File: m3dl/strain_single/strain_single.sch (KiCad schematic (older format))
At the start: 66 parts, among them IC1 AD8226, IC2 AD8541, IC3 AD8226, IC4 AD8541, IC5 AD8656, IC6 AD8226, IC7 AD8541, IC8 AD8656, IC9 AD8656, J1 WEST TOP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

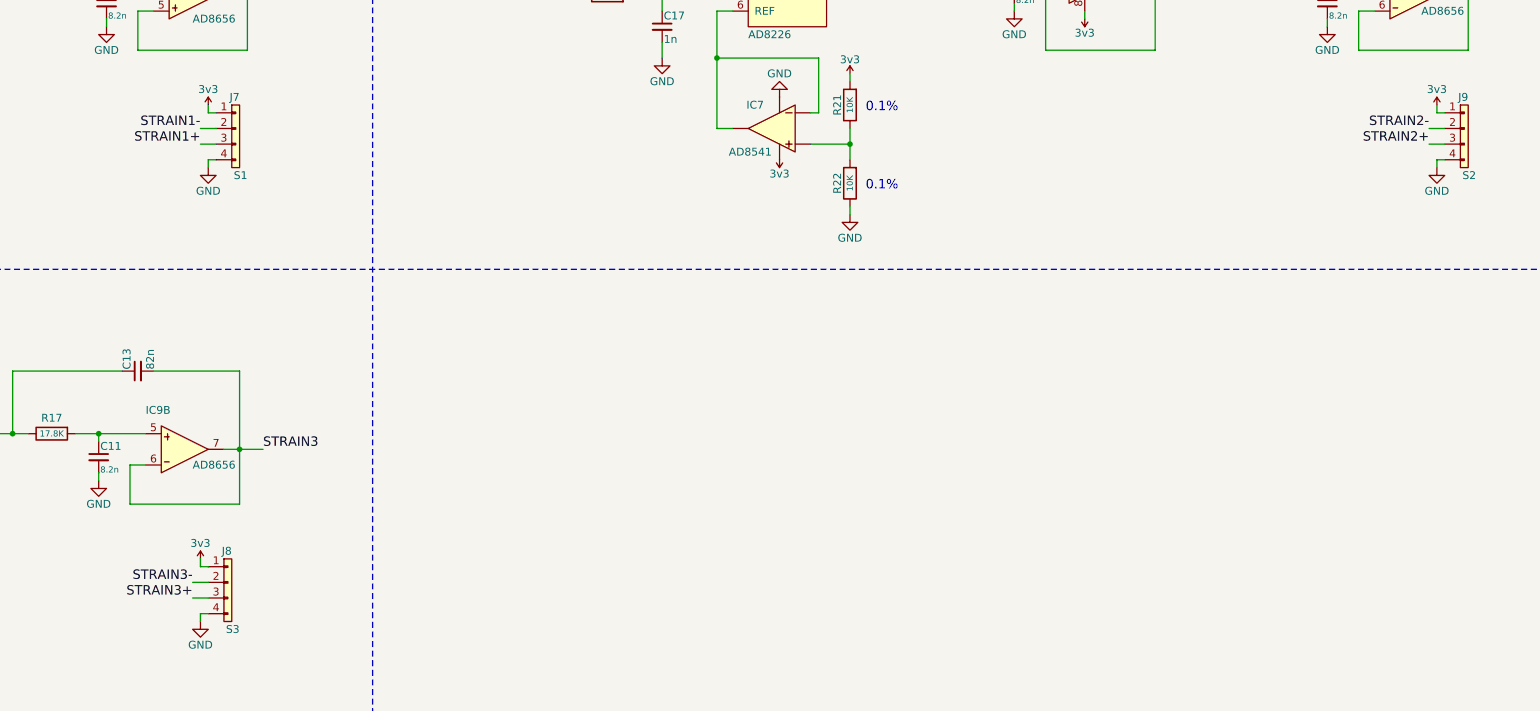
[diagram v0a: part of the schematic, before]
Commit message: Started Strain Gauge PCB Layout
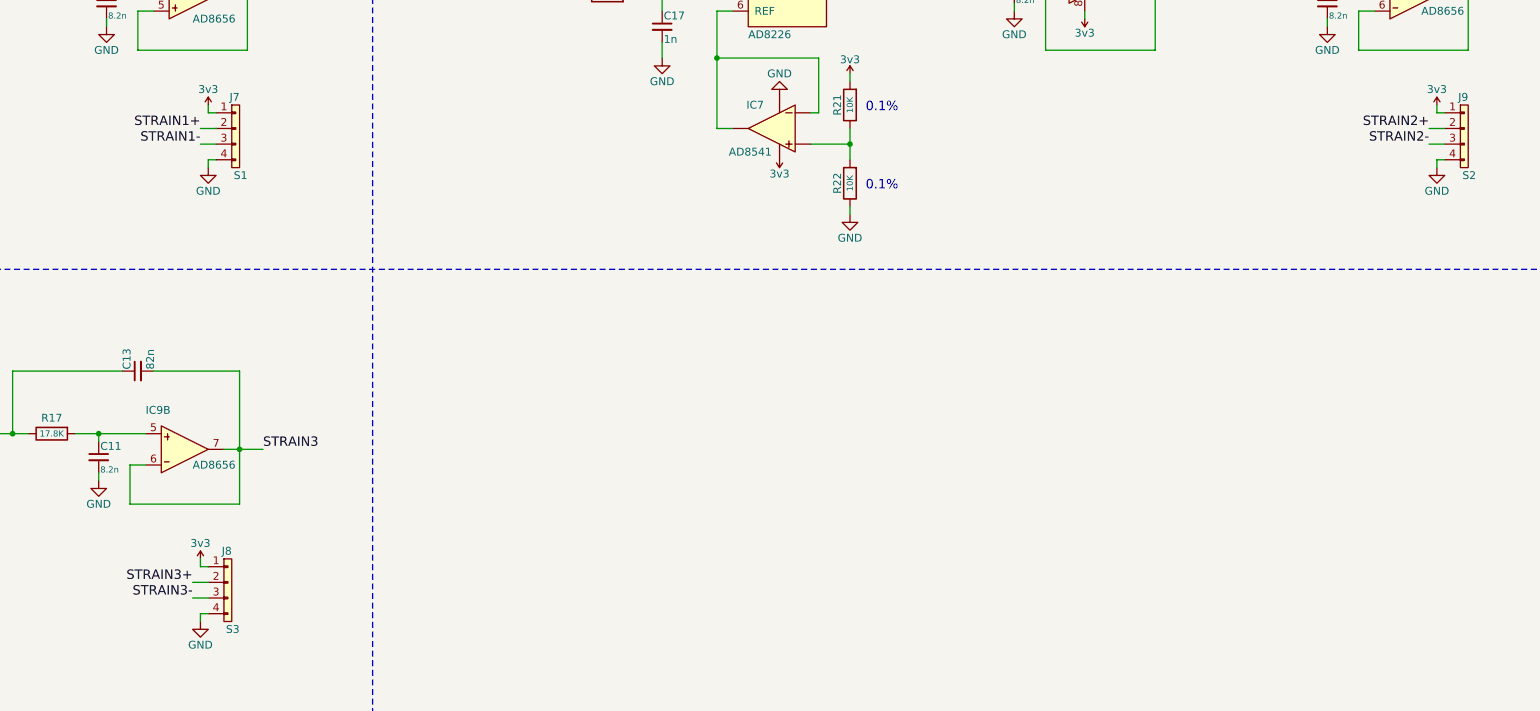
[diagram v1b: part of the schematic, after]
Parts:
- J7, J8, J9: footprint Connectors_Molex:Connector_Molex_PicoBlade_53047-0410 -> Connectors_Molex:Connector_Molex_PicoBlade_53048-0410
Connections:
- net STRAIN1+: now also J7.2; no longer J7.3
- net STRAIN1-: now also J7.3; no longer J7.2
- net STRAIN2+: now also J9.2; no longer J9.3
- net STRAIN2-: now also J9.3; no longer J9.2
- net STRAIN3+: now also J8.2; no longer J8.3
- net STRAIN3-: now also J8.3; no longer J8.2

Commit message: Finished routing Strain Gauge PCB - Needs Silkscreen
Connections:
- net STRAIN1: now also IC5.6 (-IN); no longer IC5.5 (+IN)
- net at C12.1, R18.2: now also IC5.5 (+IN); no longer IC5.6 (-IN)
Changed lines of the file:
@@
 F 4 "1858055" H 6950 1150 50  0001 L CNN "Farnell"
 	2    6950 1650
-	1    0    0    -1
+	1    0    0    1
 $EndComp
 Text Label 1550 1450 2    60   ~ 0

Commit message: Finished routing Pressure PCB - Needs Silkscreen
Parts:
- J5: value NORTH TOP -> SOUTH TOP
- J6: value NORTH BOT -> SOUTH BOT
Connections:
- net JTDO is gone; now on net JTDI: J1.8
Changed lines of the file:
@@
 P 7450 7150
 F 0 "J5" H 7350 7250 50  0000 L CNN
-F 1 "NORTH TOP" H 7400 6150 50  0000 C CNN
+F 1 "SOUTH TOP" H 7400 6150 50  0000 C CNN
 F 2 "agg:TFML-110-02-L-D" H 7450 7150 50  0001 C CNN
 F 3 "" H 7450 7150 50  0001 C CNN
@@
 P 9150 7150
 F 0 "J6" H 9050 7250 50  0000 L CNN
-F 1 "NORTH BOT" H 9100 6150 50  0000 C CNN
+F 1 "SOUTH BOT" H 9100 6150 50  0000 C CNN
 F 2 "agg:SFML-110-02-L-D-LC" H 9150 7150 50  0001 C CNN
 F 3 "" H 9150 7150 50  0001 C CNN
@@
 Text Notes 3550 5800 0    60   ~ 0
 0.1%
+Text Label 3600 8250 0    60   ~ 0
+JTDO
+Text Label 3450 8250 2    60   ~ 0
+JTDI
+Wire Wire Line
+	3450 8250 3600 8250
 $EndSCHEMATC
